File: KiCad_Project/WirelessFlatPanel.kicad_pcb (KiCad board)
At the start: 2 copper layers, 86 x 55.9 mm, 18 parts, among them U3V16F6 U3V16F6

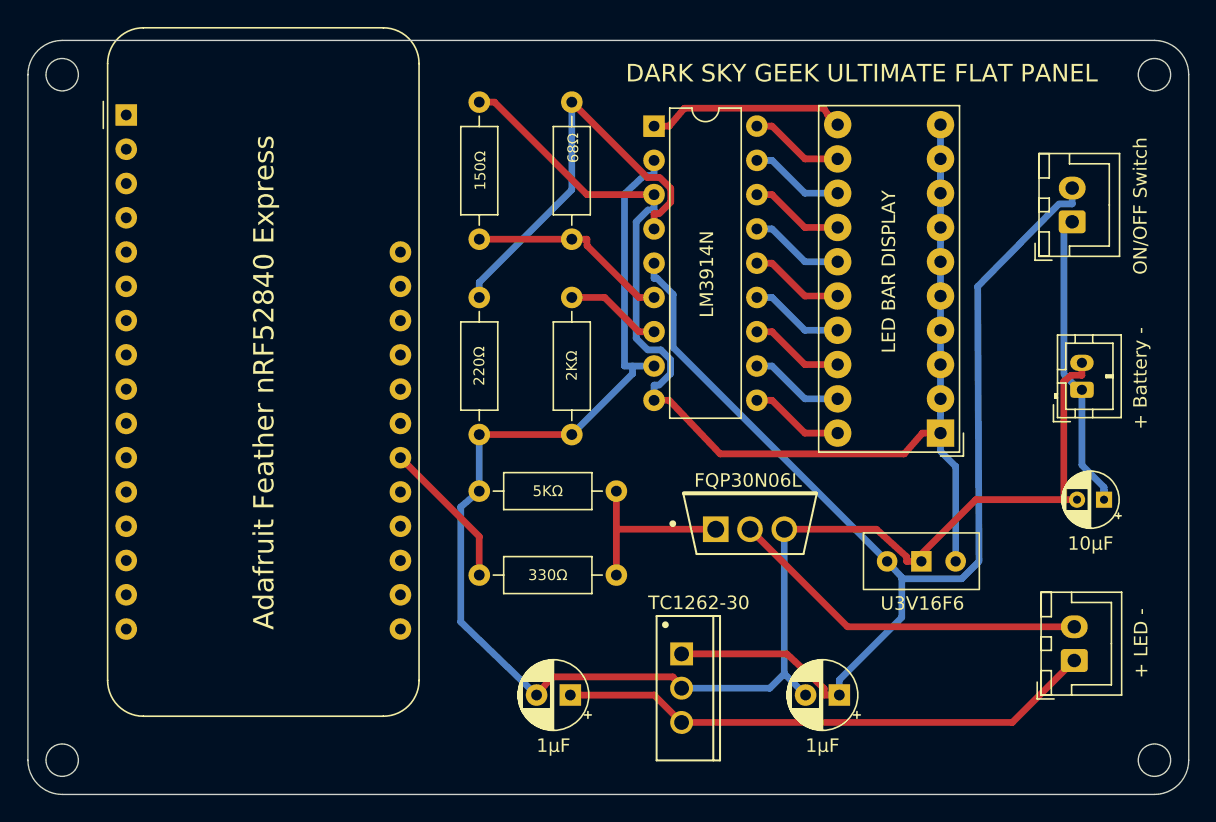
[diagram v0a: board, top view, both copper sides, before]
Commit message: Updated KiCad project to greatly simplify wiring
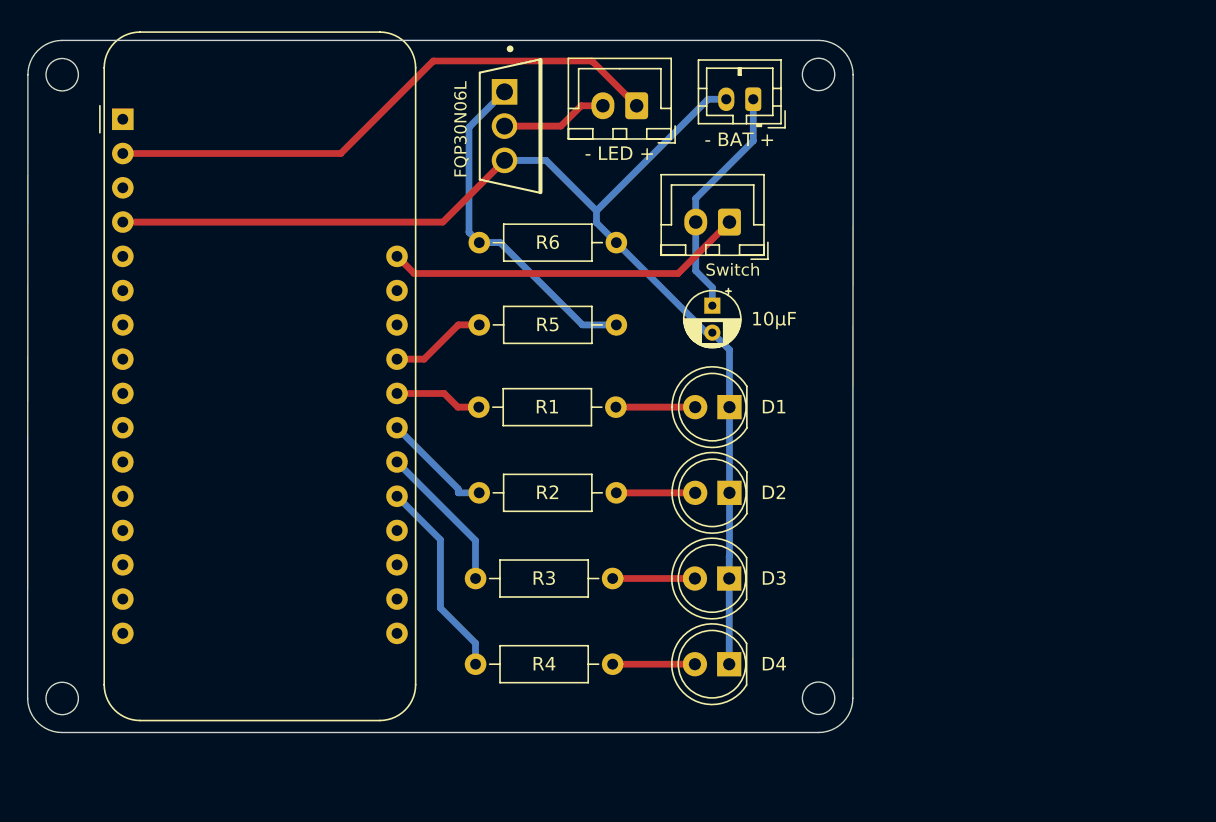
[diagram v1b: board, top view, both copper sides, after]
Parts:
- removed + Battery -: Battery, Connector_JST:JST_PH_B2B-PH-K_1x02_P2.00mm_Vertical
- removed + LED -: LED, Connector_JST:JST_XH_B2B-XH-A_1x02_P2.50mm_Vertical
- removed 150Ω: 150Ω, Resistor_THT:R_Axial_DIN0207_L6.3mm_D2.5mm_P10.16mm_Horizontal
- removed 1µF (x2): 1µF, Capacitor_THT:CP_Radial_D5.0mm_P2.50mm
- removed 220Ω: 220Ω, Resistor_THT:R_Axial_DIN0207_L6.3mm_D2.5mm_P10.16mm_Horizontal
- removed 2KΩ: 2KΩ, Resistor_THT:R_Axial_DIN0207_L6.3mm_D2.5mm_P10.16mm_Horizontal
- removed 330Ω: 330Ω, Resistor_THT:R_Axial_DIN0207_L6.3mm_D2.5mm_P10.16mm_Horizontal
- removed 5KΩ: 5KΩ, Resistor_THT:R_Axial_DIN0207_L6.3mm_D2.5mm_P10.16mm_Horizontal
- removed 68Ω: 68Ω, Resistor_THT:R_Axial_DIN0207_L6.3mm_D2.5mm_P10.16mm_Horizontal
- removed Adafruit Feather nRF52840 Express: Adafruit Feather nRF52840 Express, Module:Adafruit_Feather
- removed FQP30N06L: FQP30N06L, footprints:FQP30N06L
- removed LED BAR DISPLAY: LED Bar Display, Display:HDSP-4830
- removed LM3914N: LM3914N, Package_DIP:DIP-18_W7.62mm
- removed ON/OFF Switch: ON/OFF Switch, Connector_JST:JST_XH_B2B-XH-A_1x02_P2.50mm_Vertical
- removed TC1262-30: TC1262-30, footprints:TC1262-3.0VAB
- removed U3V16F6: U3V16F6, footprints:U3V16F6
- added - BAT +: JST-PH Bat, Connector_JST:JST_PH_B2B-PH-K_1x02_P2.00mm_Vertical, F.Cu at (155.7, 65.3)
- added - LED +: JST-XH LED, Connector_JST:JST_XH_B2B-XH-A_1x02_P2.50mm_Vertical, F.Cu at (147.0, 65.8)
- added A1: Adafruit Feather nRF52840 Express, Module:Adafruit_Feather, F.Cu at (109.0, 66.8)
- added D1: LED, LED_THT:LED_D5.0mm, F.Cu at (153.9, 88.1)
- added D2: LED, LED_THT:LED_D5.0mm, F.Cu at (153.9, 94.5)
- added D3: LED, LED_THT:LED_D5.0mm, F.Cu at (153.9, 100.8)
- added D4: LED, LED_THT:LED_D5.0mm, F.Cu at (153.9, 107.2)
- added Q1: FQP30N06L, footprints:FQP30N06L, F.Cu at (137.7, 67.3)
- added R1: 330Ω, Resistor_THT:R_Axial_DIN0207_L6.3mm_D2.5mm_P10.16mm_Horizontal, F.Cu at (145.5, 88.1)
- added R2: 330Ω, Resistor_THT:R_Axial_DIN0207_L6.3mm_D2.5mm_P10.16mm_Horizontal, F.Cu at (145.5, 94.5)
- added R3: 330Ω, Resistor_THT:R_Axial_DIN0207_L6.3mm_D2.5mm_P10.16mm_Horizontal, F.Cu at (145.3, 100.8)
- added R4: 330Ω, Resistor_THT:R_Axial_DIN0207_L6.3mm_D2.5mm_P10.16mm_Horizontal, F.Cu at (145.3, 107.2)
- added R5: 330Ω, Resistor_THT:R_Axial_DIN0207_L6.3mm_D2.5mm_P10.16mm_Horizontal, F.Cu at (145.5, 82.0)
- added R6: 5KΩ, Resistor_THT:R_Axial_DIN0207_L6.3mm_D2.5mm_P10.16mm_Horizontal, F.Cu at (145.5, 75.9)
- added Switch: JST-XH Switch, Connector_JST:JST_XH_B2B-XH-A_1x02_P2.50mm_Vertical, F.Cu at (153.9, 74.4)
- moved 10µF 32.4 mm to (152.7, 80.6), turned to -90 degrees
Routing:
- net +6V: track 97.8 -> 0.00 mm
- net VCC: track 92.5 -> 0.00 mm
- net Net-(A1-Pad2): track 0.00 -> 42.3 mm
- net +3V0: track 40.1 -> 0.00 mm
- net GND: track 124.2 -> 89.5 mm
- net Net-(R2-Pad1): track 30.8 -> 0.00 mm
- net Net-(J2-Pad2): track 27.0 -> 0.00 mm
- net Net-(A1-Pad28): track 0.00 -> 26.7 mm
- net Net-(BAR1-Pad11): track 15.2 -> 0.00 mm
- net Net-(R1-Pad1): track 15.0 -> 0.00 mm
- net Net-(A1-Pad21): track 0.00 -> 14.9 mm
- net Net-(Q1-Pad1): track 13.6 -> 25.3 mm
- net Net-(A1-Pad23): track 0.00 -> 8.26 mm
- net Net-(Q1-Pad2): track 0.00 -> 7.91 mm
- net Net-(R5-Pad2): track 0.00 -> 7.15 mm
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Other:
- board size 86 x 55.9 mm -> 61.2 x 51.3 mm

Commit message: Updated PCB footprint
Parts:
- Q1: value FQP30N06L -> Val**
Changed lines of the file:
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@@
       (effects (font (size 1 1) (thickness 0.15)) (justify left))
     )
-    (fp_text value "FQP30N06L" (at -3.6515 0.254 90) (layer "F.SilkS")
+    (fp_text value "Val**" (at -3.6515 0.254 90) (layer "F.SilkS") hide
       (effects (font (size 0.9 0.9) (thickness 0.15)))
     )
+    (fp_line (start -2.25 -3.96) (end -2.25 3.96) (layer "F.SilkS") (width 0.15))
+    (fp_line (start 2.25 -4.95) (end -2.25 -3.96) (layer "F.SilkS") (width 0.15))
+    (fp_line (start -2.25 3.96) (end 2.25 4.95) (layer "F.SilkS") (width 0.15))
     (fp_line (start 2.25 4.9) (end 2.25 -4.9) (layer "F.SilkS") (width 0.3))
-    (fp_line (start 2.25 -4.95) (end -2.25 -3.96) (layer "F.SilkS") (width 0.15))
-    (fp_line (start -2.25 -3.96) (end -2.25 3.96) (layer "F.SilkS") (width 0.15))
-    (fp_line (start -2.25 3.96) (end 2.25 4.95) (layer "F.SilkS") (width 0.15))
     (fp_circle (center 0 -5.725) (end 0.125 -5.725) (layer "F.SilkS") (width 0.25) (fill none))
     (fp_line (start -2.375 -5.075) (end -2.375 5.075) (layer "F.CrtYd") (width 0.15))
+    (fp_line (start 2.375 5.075) (end 2.375 -5.075) (layer "F.CrtYd") (width 0.15))
+    (fp_line (start -2.375 5.075) (end 2.375 5.075) (layer "F.CrtYd") (width 0.15))
     (fp_line (start 2.375 -5.075) (end -2.375 -5.075) (layer "F.CrtYd") (width 0.15))
-    (fp_line (start -2.375 5.075) (end 2.375 5.075) (layer "F.CrtYd") (width 0.15))
-    (fp_line (start 2.375 5.075) (end 2.375 -5.075) (layer "F.CrtYd") (width 0.15))
     (fp_line (start 2.375 -5.075) (end 2.375 -5.075) (layer "F.CrtYd") (width 0.15))
+    (fp_line (start -2.25 4.95) (end -2.25 -4.95) (layer "F.Fab") (width 0.15))
     (fp_line (start 2.25 4.95) (end -2.25 4.95) (layer "F.Fab") (width 0.15))
-    (fp_line (start -2.25 4.95) (end -2.25 -4.95) (layer "F.Fab") (width 0.15))
+    (fp_line (start 2.25 -4.95) (end 2.25 4.95) (layer "F.Fab") (width 0.15))
     (fp_line (start -2.25 -4.95) (end 2.25 -4.95) (layer "F.Fab") (width 0.15))
-    (fp_line (start 2.25 -4.95) (end 2.25 4.95) (layer "F.Fab") (width 0.15))
-    (pad "1" thru_hole rect (at -0.4125 -2.54) (size 1.9 1.9) (drill 1.25) (layers *.Cu)
+    (pad "1" thru_hole rect (at -0.4125 -2.54) (size 1.9 1.9) (drill 1.25) (layers *.Cu "F.Mask")
       (net 34 "Net-(Q1-Pad1)") (pinfunction "G") (pintype "unspecified") (thermal_width 0.45))
-    (pad "2" thru_hole circle (at -0.4125 0) (size 1.9 1.9) (drill 1.25) (layers *.Cu)
+    (pad "2" thru_hole circle (at -0.4125 0) (size 1.9 1.9) (drill 1.25) (layers *.Cu "F.Mask")
       (net 33 "Net-(Q1-Pad2)") (pinfunction "D") (pintype "unspecified") (thermal_width 0.45))
-    (pad "3" thru_hole circle (at -0.4125 2.54) (size 1.9 1.9) (drill 1.25) (layers *.Cu)
+    (pad "3" thru_hole circle (at -0.4125 2.54) (size 1.9 1.9) (drill 1.25) (layers *.Cu "F.Mask")
       (net 28 "GND") (pinfunction "S") (pintype "unspecified") (thermal_width 0.45))
     (model "/Users/jlecomte/Documents/KiCad/6.0/3dmodels/FQP30N06L.step"
